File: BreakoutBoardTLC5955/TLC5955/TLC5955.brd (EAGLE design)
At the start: 30.5 x 71.1 mm, 4 parts

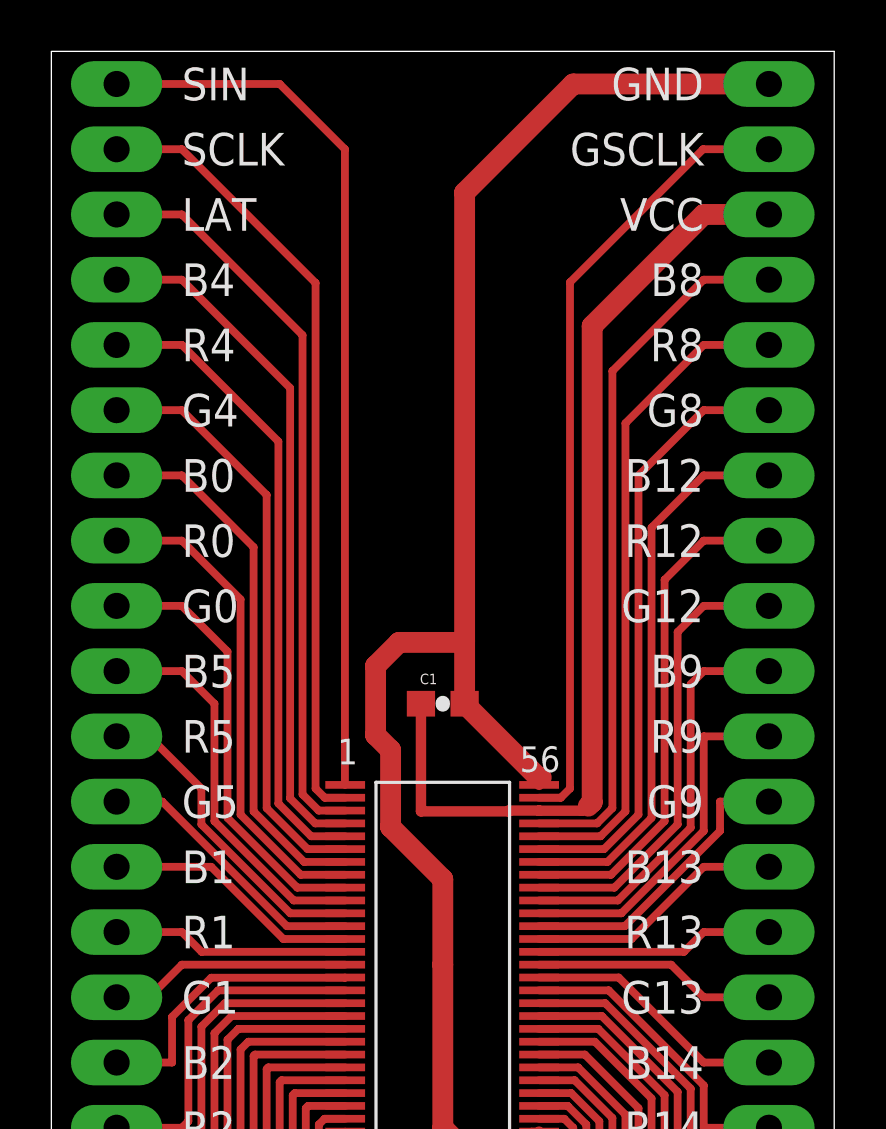
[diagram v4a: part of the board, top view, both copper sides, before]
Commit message: Small trace changes on TI5955 for more compact traces.
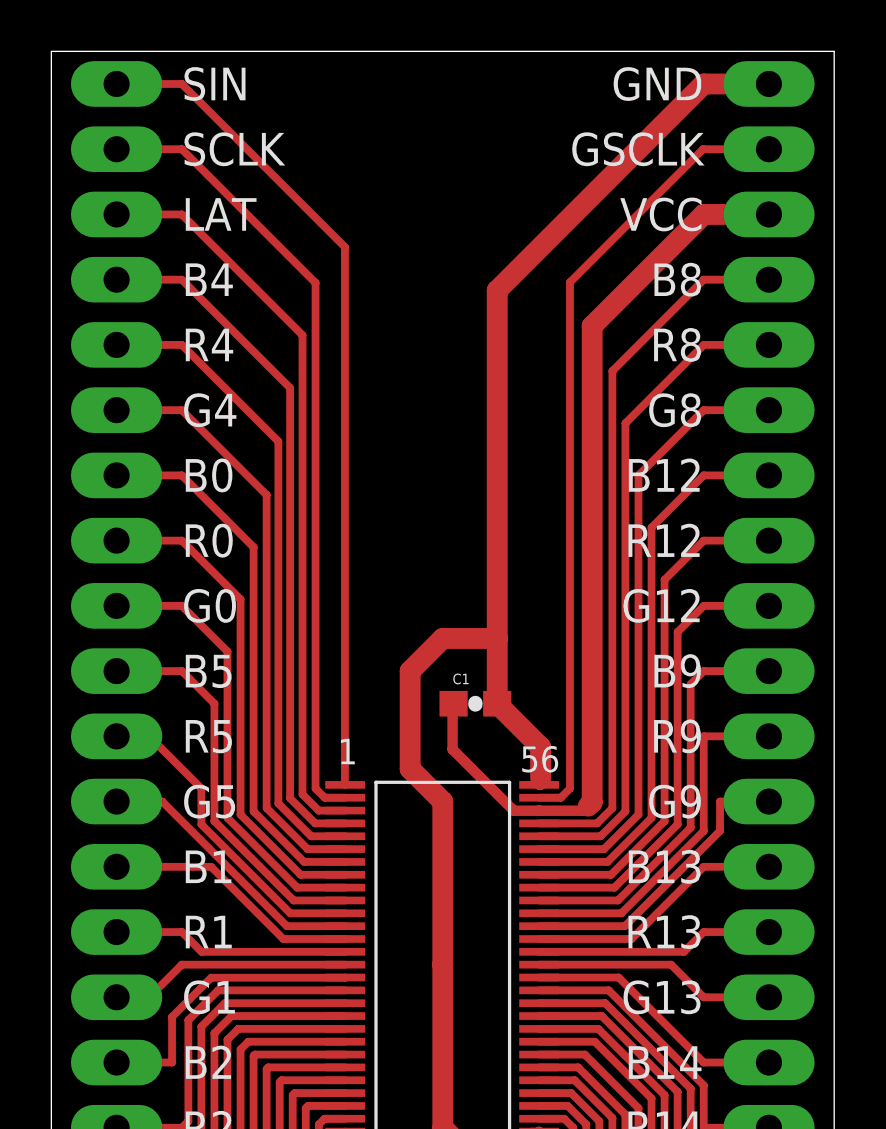
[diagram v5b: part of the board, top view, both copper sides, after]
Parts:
- moved C1 1.27 mm to (16.5, 45.7)
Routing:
- net N$57: track 98.0 -> 93.2 mm
- net N$31: track 38.3 -> 35.6 mm
- net N$26: track 34.7 -> 32.5 mm
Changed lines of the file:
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@@
 <element name="U$2" library="WallerLabLib" package="28PIN_HOLES" value="28_PINS0" x="2.54" y="35.56" rot="R270"/>
 <element name="U$3" library="WallerLabLib" package="28PIN_HOLES" value="28_PINS0" x="27.94" y="35.56" rot="R90"/>
-<element name="C1" library="WallerLabLib" package="0603-CAP" value="10uF" x="15.24" y="45.72">
-<attribute name="PROD_ID" value="CAP-11015" x="15.24" y="45.72" size="1.778" layer="27" display="off"/>
+<element name="C1" library="WallerLabLib" package="0603-CAP" value="10uF" x="16.51" y="45.72">
+<attribute name="PROD_ID" value="CAP-11015" x="16.51" y="45.72" size="1.778" layer="27" display="off"/>
 </element>
 </elements>
@@
 <contactref element="U$2" pad="P1"/>
 <contactref element="U$1" pad="P1"/>
-<wire x1="2.54" y1="69.85" x2="8.89" y2="69.85" width="0.3048" layer="1"/>
-<wire x1="8.89" y1="69.85" x2="11.43" y2="67.31" width="0.3048" layer="1"/>
 <wire x1="11.43" y1="42.57" x2="11.44" y2="42.56" width="0.3048" layer="1"/>
-<wire x1="11.43" y1="67.31" x2="11.43" y2="42.57" width="0.3048" layer="1"/>
+<wire x1="11.43" y1="63.5" x2="11.43" y2="42.57" width="0.3048" layer="1"/>
+<wire x1="11.43" y1="63.5" x2="5.08" y2="69.85" width="0.3048" layer="1"/>
+<wire x1="5.08" y1="69.85" x2="2.54" y2="69.85" width="0.3048" layer="1"/>
 </signal>
 <signal name="N$27">
@@
 <contactref element="U$3" pad="P26"/>
 <contactref element="C1" pad="1"/>
-<wire x1="18.99" y1="41.56" x2="17.8054" y2="41.56" width="0.4064" layer="1"/>
-<wire x1="17.8054" y1="41.56" x2="17.8054" y2="41.529" width="0.4064" layer="1"/>
-<wire x1="17.8054" y1="41.529" x2="14.39" y2="41.529" width="0.4064" layer="1"/>
-<wire x1="14.39" y1="41.529" x2="14.39" y2="45.72" width="0.4064" layer="1"/>
 <wire x1="21.0566" y1="41.8846" x2="21.0566" y2="60.4266" width="0.8128" layer="1"/>
 <wire x1="21.0566" y1="60.4266" x2="25.4" y2="64.77" width="0.8128" layer="1"/>
@@
 <wire x1="20.6502" y1="41.5544" x2="18.9956" y2="41.5544" width="0.4064" layer="1"/>
 <wire x1="18.9956" y1="41.5544" x2="18.99" y2="41.56" width="0.4064" layer="1"/>
+<wire x1="18.9956" y1="41.5544" x2="18.0086" y2="41.5544" width="0.4064" layer="1"/>
+<wire x1="18.0086" y1="41.5544" x2="15.621" y2="43.942" width="0.4064" layer="1"/>
+<wire x1="15.621" y1="43.942" x2="15.621" y2="45.681" width="0.4064" layer="1"/>
+<wire x1="15.621" y1="45.681" x2="15.66" y2="45.72" width="0.4064" layer="1"/>
 </signal>
 <signal name="N$33">
@@
 <wire x1="15.6972" y1="28.7528" x2="15.24" y2="29.21" width="0.8128" layer="1"/>
 <wire x1="15.24" y1="29.21" x2="15.24" y2="35.56" width="0.8128" layer="1"/>
-<wire x1="18.99" y1="42.56" x2="18.99" y2="42.7644" width="0.4064" layer="1"/>
-<wire x1="18.99" y1="42.7644" x2="19.0754" y2="42.8498" width="0.4064" layer="1"/>
-<wire x1="19.0754" y1="42.8498" x2="18.9602" y2="42.8498" width="0.8128" layer="1"/>
-<wire x1="18.9602" y1="42.8498" x2="16.09" y2="45.72" width="0.8128" layer="1"/>
-<wire x1="16.09" y1="45.72" x2="16.09" y2="48.1584" width="0.8128" layer="1"/>
-<wire x1="16.09" y1="48.1584" x2="16.09" y2="65.62" width="0.8128" layer="1"/>
-<wire x1="16.09" y1="65.62" x2="20.32" y2="69.85" width="0.8128" layer="1"/>
-<wire x1="20.32" y1="69.85" x2="27.94" y2="69.85" width="0.8128" layer="1"/>
-<wire x1="15.24" y1="35.56" x2="15.24" y2="38.8874" width="0.8128" layer="1"/>
-<wire x1="15.24" y1="38.8874" x2="13.208" y2="40.9194" width="0.8128" layer="1"/>
-<wire x1="13.208" y1="40.9194" x2="13.208" y2="43.9166" width="0.8128" layer="1"/>
-<wire x1="13.208" y1="43.9166" x2="12.6238" y2="44.5008" width="0.8128" layer="1"/>
-<wire x1="12.6238" y1="44.5008" x2="12.6238" y2="47.1932" width="0.8128" layer="1"/>
-<wire x1="12.6238" y1="47.1932" x2="13.5382" y2="48.1076" width="0.8128" layer="1"/>
-<wire x1="13.5382" y1="48.1076" x2="16.0392" y2="48.1076" width="0.8128" layer="1"/>
-<wire x1="16.0392" y1="48.1076" x2="16.09" y2="48.1584" width="0.8128" layer="1"/>
+<wire x1="18.99" y1="42.56" x2="19.05" y2="42.56" width="0.4064" layer="1"/>
+<wire x1="19.05" y1="42.56" x2="19.05" y2="42.799" width="0.4064" layer="1"/>
+<wire x1="19.05" y1="42.799" x2="19.05" y2="44.03" width="0.8128" layer="1"/>
+<wire x1="19.05" y1="44.03" x2="17.36" y2="45.72" width="0.8128" layer="1"/>
+<wire x1="17.36" y1="45.72" x2="17.36" y2="48.26" width="0.8128" layer="1"/>
+<wire x1="17.36" y1="48.26" x2="17.36" y2="61.81" width="0.8128" layer="1"/>
+<wire x1="17.36" y1="61.81" x2="25.4" y2="69.85" width="0.8128" layer="1"/>
+<wire x1="25.4" y1="69.85" x2="27.94" y2="69.85" width="0.8128" layer="1"/>
+<wire x1="15.24" y1="35.56" x2="15.24" y2="41.91" width="0.8128" layer="1"/>
+<wire x1="15.24" y1="41.91" x2="13.97" y2="43.18" width="0.8128" layer="1"/>
+<wire x1="13.97" y1="43.18" x2="13.97" y2="46.99" width="0.8128" layer="1"/>
+<wire x1="13.97" y1="46.99" x2="15.24" y2="48.26" width="0.8128" layer="1"/>
+<wire x1="15.24" y1="48.26" x2="17.36" y2="48.26" width="0.8128" layer="1"/>
 </signal>
 </signals>
